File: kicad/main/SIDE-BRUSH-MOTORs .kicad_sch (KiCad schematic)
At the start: 9 parts, among them J15 SIDE BRUSH, U18 DRV8870DDAR

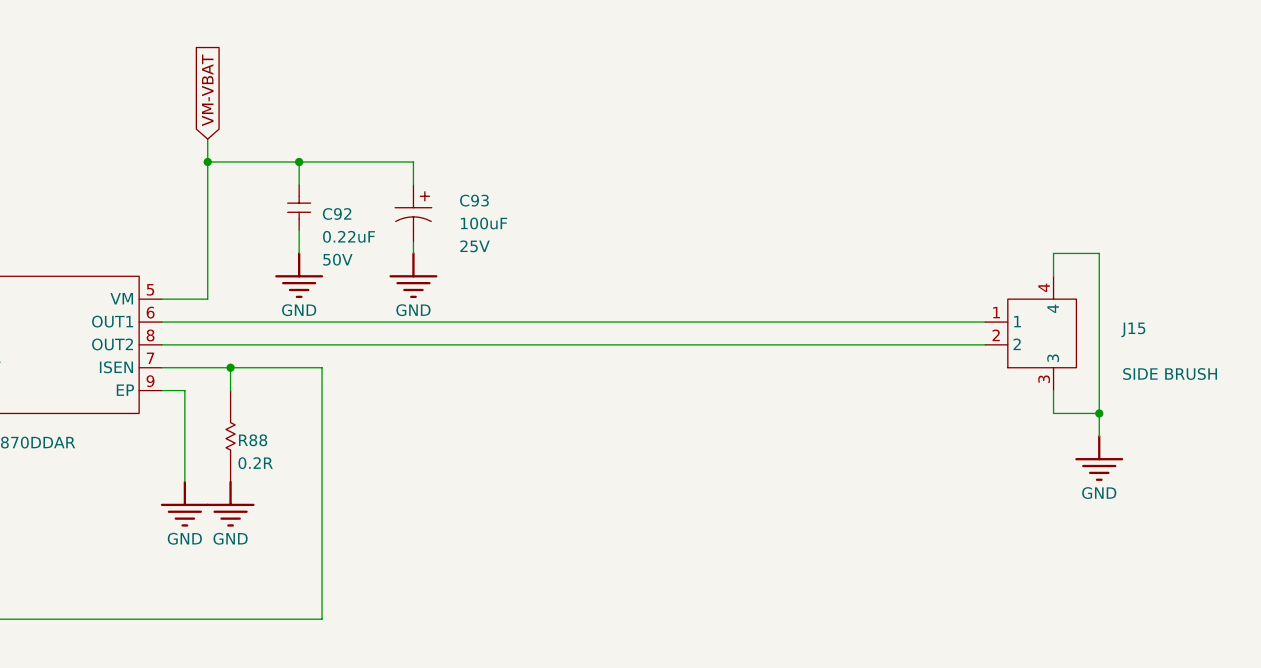
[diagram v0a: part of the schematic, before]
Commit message: Fix edge cut; no-CM STEP
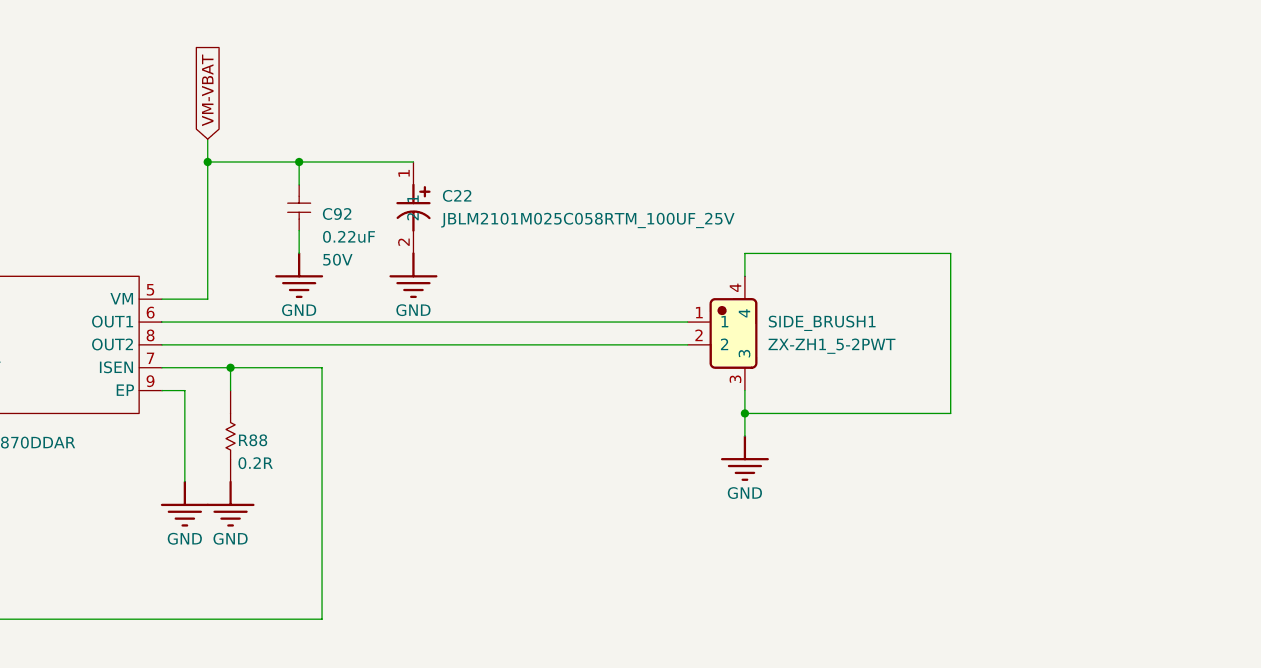
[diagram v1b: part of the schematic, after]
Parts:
- removed C93: 100uF, oomwoo_altium:CAP-SMD_BD6.3-L6.6-W6.6-FD, symbol DesignLibrary:WHEEL MOTOR_3_Capacitor-2_DesignLibrary.SchLib
- removed J15: SIDE BRUSH, oomwoo_altium:CONN-SMD_2P-P1.50_ZX-ZH1.5-2PWT, symbol DesignLibrary:SIDE-BRUSH_0_HDRx2_DesignLibrary.SchLib
- added C22: JBLM2101M025C058RTM_100UF_25V, JLCImport:JBLM2101M025C058RTM_100UF_25V, symbol JLCImport:JBLM2101M025C058RTM_100UF_25V
- added SIDE_BRUSH1: ZX-ZH1_5-2PWT, JLCImport:ZX-ZH1_5-2PWT, symbol JLCImport:ZX-ZH1_5-2PWT
- R88: footprint Resistor_SMD:R_0603_1608Metric -> Resistor_SMD:R_2512_6332Metric
- U18: footprint oomwoo_altium:HSOP-8_L5.0-W4.0-P1.27-LS6.2-BL-EP -> JLCImport:DRV8870DDAR
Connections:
- net GND: now also C22.2, SIDE_BRUSH1.3, SIDE_BRUSH1.4
- net VM-VBAT: now also C22.1
- net at U18.6 (OUT1): now also SIDE_BRUSH1.1
- net at U18.8 (OUT2): now also SIDE_BRUSH1.2

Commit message: Schematic fixes, 1st round of review
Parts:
- removed C22: JBLM2101M025C058RTM_100UF_25V, JLCImport:JBLM2101M025C058RTM_100UF_25V, symbol JLCImport:JBLM2101M025C058RTM_100UF_25V
- removed R105, R91: 10K, Resistor_SMD:R_0603_1608Metric, symbol DesignLibrary:WHEEL MOTOR_0_Resistor-1_DesignLibrary.SchLib
- added C138: 10uF/25V, Capacitor_SMD:C_0603_1608Metric, symbol JLCImport:CL21A106KBYQNNE
- added R55, R57: 100k, Resistor_SMD:R_0603_1608Metric, symbol Device:R_US
- C92: value 0.22uF -> 100nF/50V; LCSC (none) -> C1591; MANUFACTURER * -> (none); Manufacturer (none) -> *
- D22: LCSC (none) -> C2892681; MANUFACTURER * -> (none); Manufacturer (none) -> *
- R110: value 10K -> 10k; MANUFACTURER * -> (none); Manufacturer (none) -> *
- R88: value 0.2R -> 0.2R/10W; LCSC (none) -> C5375488; MANUFACTURER * -> (none); Manufacturer (none) -> *
- U18: LCSC (none) -> C86590; MANUFACTURER * -> (none); Manufacturer (none) -> *
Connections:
- net GND: now also C138.2, R55.2, R57.2
- net SIDE-BRUSH-IN1: now also U18.3 (IN1), R55.1
- net SIDE-BRUSH-IN2: now also U18.2 (IN2), R57.1
- net VM-VBAT: now also C138.1
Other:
- moved on the sheet: C92, D22, R110, R88, SIDE_BRUSH1, U18
